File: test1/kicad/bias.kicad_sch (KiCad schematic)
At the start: 15 parts, among them Q40 PMZ1200UPEYL, Q41 PMZ1200UPEYL, Q42 2N7002, Q43 2N7002, U40 MCP4728, U41 OPA2388

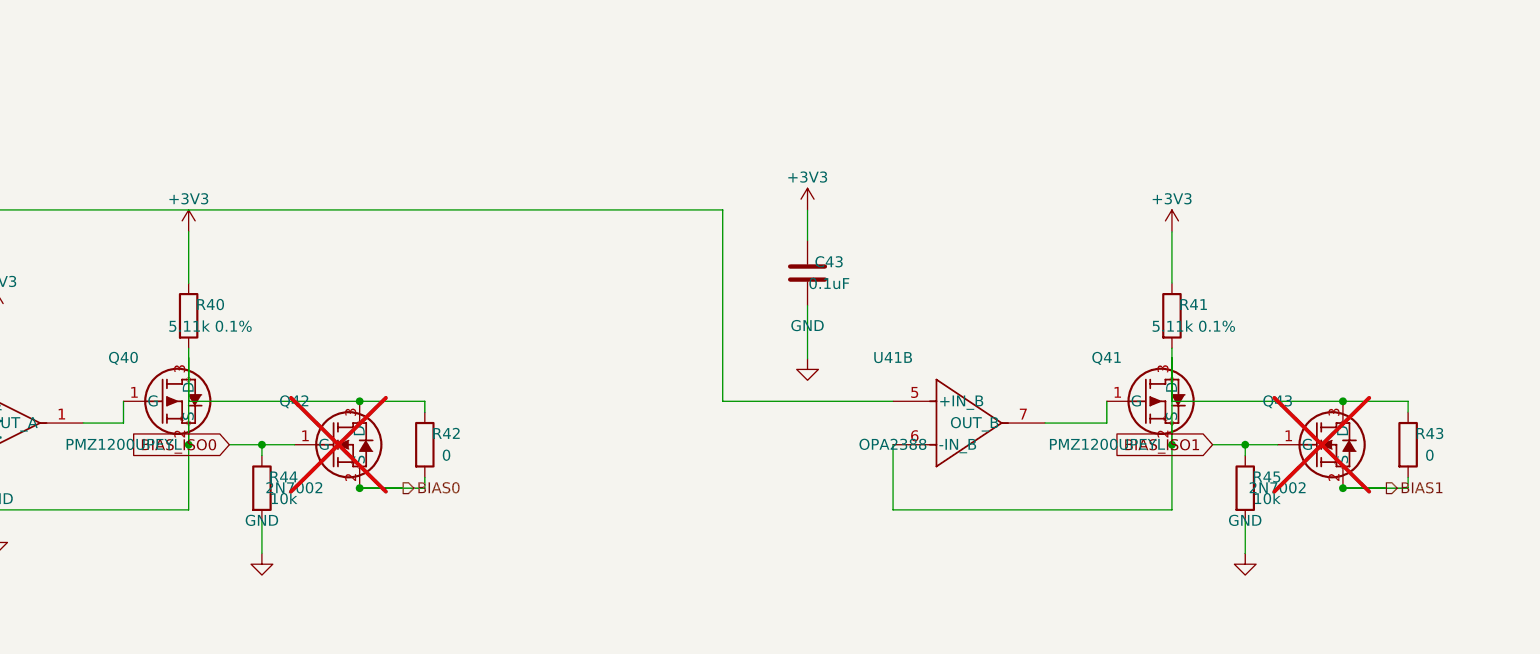
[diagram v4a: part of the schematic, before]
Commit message: Add layout linter + cluster helpers; fix silent shorts across sheets
Introduces gen/layout_lint.py with checks for bbox spacing, wires
through/into a body, parallel-wire overlap on the same axis, bridged
drop columns, and dense GND clusters — non-fatal warnings the strict
validator cannot catch (each net's name is still present in a bridged
component's name set, so per-member name checks pass).

Fixes the bugs the linter exposed:
- FMC routing flipped to exit LEFT (pin-protrusion side) so wires no
  longer pass through the connector body
- bobcat OWT (pins 23-25) + GPIO (37-40) get one drop column per pin,
  ending the silent shorts between adjacent nets
- bobcat SPI pin 14 pull-x shifted off pin 19's column
- bias Q40/Q41 source/drain wires detoured around the body so source
  no longer shorts to drain through the same vertical
- power LDO redundant tap stubs + GND-rail dupes removed; C12 moved
  off R10's column so NR_SS doesn't short to GND
- C11 ↔ R10, J54-56 ↔ R50-52 spacing widened to meet bbox rule

Adds gnd_bus() and decoupling_cluster() helpers in gen/shared.py and
applies gnd_bus() to the eeprom address-strap pins.

Skill doc gets rules for pin-protrusion side, per-pin drop columns,
and same-axis wire overlap. All 7 sheets now pass kicad-cli parse,
the strict connectivity validator, and the layout linter.

Co-Authored-By: Claude Opus 4.7 (1M context) <noreply@anthropic.com>
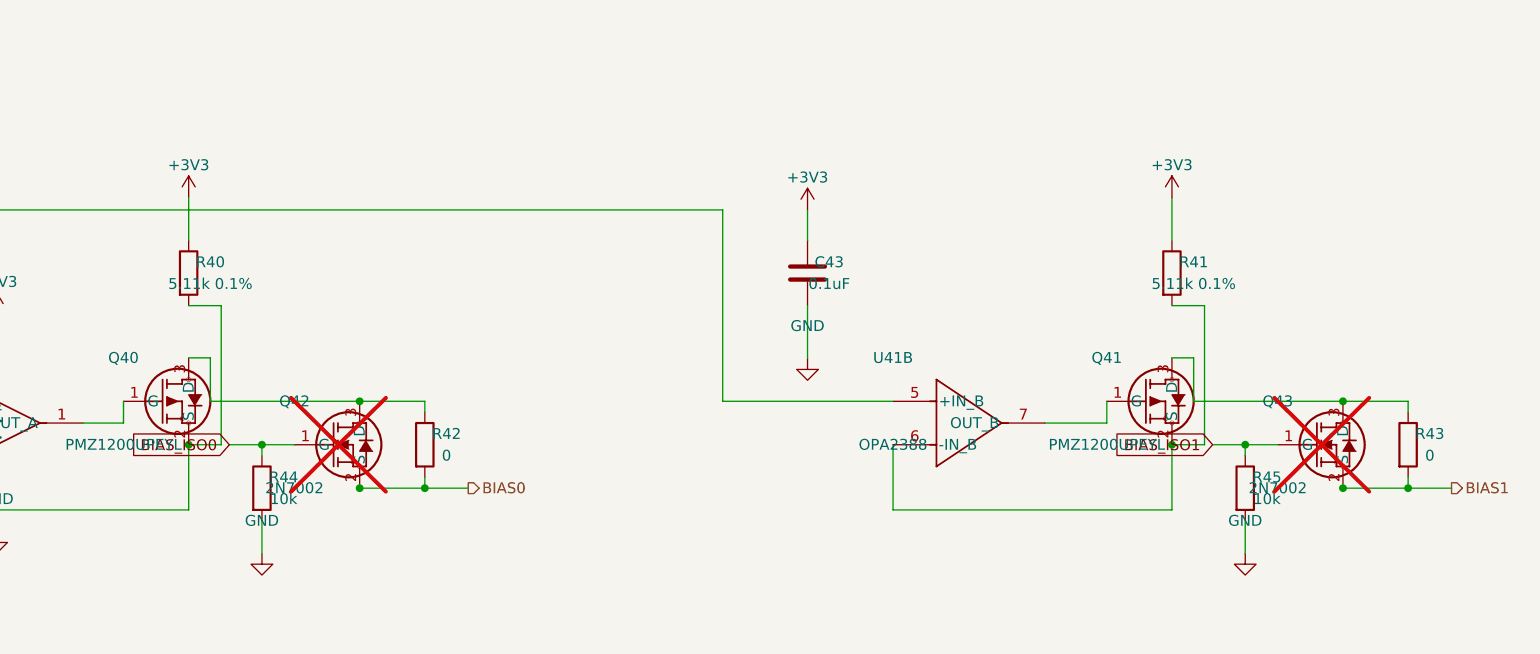
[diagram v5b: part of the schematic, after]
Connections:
- net at Q40.3 (D), Q42.3 (D), R42.1: no longer Q40.2 (S), R40.2, U41.2 (-IN_A)
- net at Q41.2 (S), R41.2, U41.6 (-IN_B): no longer Q41.3 (D), Q43.3 (D), R43.1
- new net: Q41.3 (D), Q43.3 (D), R43.1
- new net: Q40.2 (S), R40.2, U41.2 (-IN_A)
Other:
- moved on the sheet: R40, R41
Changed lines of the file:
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@@
   (symbol
     (lib_id "Device:R")
-    (at 237.62 100 0)
-    (unit 1) (in_bom yes) (on_board yes) (dnp no)
-    (property "Reference" "R40" (at 240.16 98.73 0) (effects (font (size 1.27 1.27))))
-    (property "Value" "5.11k 0.1%" (at 240.16 101.27 0) (effects (font (size 1.27 1.27))))
+    (at 237.62 95 0)
+    (unit 1) (in_bom yes) (on_board yes) (dnp no)
+    (property "Reference" "R40" (at 240.16 93.73 0) (effects (font (size 1.27 1.27))))
+    (property "Value" "5.11k 0.1%" (at 240.16 96.27 0) (effects (font (size 1.27 1.27))))
     (property "Footprint" "Resistor_SMD:R_0402_1005Metric" (at 0 0 0) (effects (font (size 1.27 1.27)) (hide yes)))
     (property "Datasheet" "" (at 0 0 0) (effects (font (size 1.27 1.27)) (hide yes)))
@@
       (project "test1"
         (path "/4ed7a046-ef33-57d9-8730-321c05965af3/ddf1c49f-55ac-530a-9ee4-38ad9d14caf8" (reference "R40") (unit 1)))))
-  (wire (pts (xy 237.62 103.81) (xy 237.62 115.08)) (stroke (width 0) (type default)))
-  (wire (pts (xy 237.62 96.19) (xy 237.62 90.17)) (stroke (width 0) (type default)))
-  (symbol
-    (lib_id "power:+3V3")
-    (at 237.62 90.17 0)
-    (unit 1) (in_bom yes) (on_board yes) (dnp no)
-    (property "Reference" "#PWR9abd0652" (at 237.62 83.82000000000001 0) (effects (font (size 1.27 1.27)) (hide yes)))
-    (property "Value" "+3V3" (at 237.62 86.36 0) (effects (font (size 1.27 1.27))))
-    (property "Footprint" "" (at 0 0 0) (effects (font (size 1.27 1.27)) (hide yes)))
-    (property "Datasheet" "" (at 0 0 0) (effects (font (size 1.27 1.27)) (hide yes)))
-    (pin "1")
-    (instances
-      (project "test1"
-        (path "/4ed7a046-ef33-57d9-8730-321c05965af3/ddf1c49f-55ac-530a-9ee4-38ad9d14caf8" (reference "#PWR9abd0652") (unit 1)))))
+  (wire (pts (xy 237.62 115.08) (xy 241.43 115.08)) (stroke (width 0) (type default)))
+  (wire (pts (xy 241.43 115.08) (xy 241.43 98.81)) (stroke (width 0) (type default)))
+  (wire (pts (xy 241.43 98.81) (xy 237.62 98.81)) (stroke (width 0) (type default)))
+  (wire (pts (xy 237.62 91.19) (xy 237.62 86.19)) (stroke (width 0) (type default)))
+  (symbol
+    (lib_id "power:+3V3")
+    (at 237.62 86.19 0)
+    (unit 1) (in_bom yes) (on_board yes) (dnp no)
+    (property "Reference" "#PWRa475a855" (at 237.62 79.84 0) (effects (font (size 1.27 1.27)) (hide yes)))
+    (property "Value" "+3V3" (at 237.62 82.38 0) (effects (font (size 1.27 1.27))))
+    (property "Footprint" "" (at 0 0 0) (effects (font (size 1.27 1.27)) (hide yes)))
+    (property "Datasheet" "" (at 0 0 0) (effects (font (size 1.27 1.27)) (hide yes)))
+    (pin "1")
+    (instances
+      (project "test1"
+        (path "/4ed7a046-ef33-57d9-8730-321c05965af3/ddf1c49f-55ac-530a-9ee4-38ad9d14caf8" (reference "#PWRa475a855") (unit 1)))))
   (wire (pts (xy 205.0 115.08) (xy 205.0 122.7)) (stroke (width 0) (type default)))
   (wire (pts (xy 205.0 122.7) (xy 237.62 122.7)) (stroke (width 0) (type default)))
@@
       (project "test1"
         (path "/4ed7a046-ef33-57d9-8730-321c05965af3/ddf1c49f-55ac-530a-9ee4-38ad9d14caf8" (reference "Q42") (unit 1)))))
-  (wire (pts (xy 237.62 104.92) (xy 237.62 110.0)) (stroke (width 0) (type default)))
-  (wire (pts (xy 237.62 110.0) (xy 257.62 110.0)) (stroke (width 0) (type default)))
-  (wire (pts (xy 257.62 120.16) (xy 262.7 120.16)) (stroke (width 0) (type default)))
-  (hierarchical_label "BIAS0" (shape output) (at 262.7 120.16 0) (effects (font (size 1.27 1.27)) (justify left)))
-  (wire (pts (xy 250.0 115.08) (xy 242.38 115.08)) (stroke (width 0) (type default)))
-  (global_label "BIAS_ISO0" (shape input) (at 242.38 115.08 180) (effects (font (size 1.27 1.27)) (justify right)))
+  (wire (pts (xy 237.62 104.92) (xy 240.16 104.92)) (stroke (width 0) (type default)))
+  (wire (pts (xy 240.16 104.92) (xy 240.16 110.0)) (stroke (width 0) (type default)))
+  (wire (pts (xy 240.16 110.0) (xy 257.62 110.0)) (stroke (width 0) (type default)))
   (symbol
     (lib_id "Device:R")
@@
   (wire (pts (xy 257.62 120.16) (xy 265.24 120.16)) (stroke (width 0) (type default)))
   (wire (pts (xy 265.24 120.16) (xy 265.24 118.89)) (stroke (width 0) (type default)))
+  (junction (at 265.24 120.16) (diameter 0) (color 0 0 0 0))
+  (wire (pts (xy 265.24 120.16) (xy 270.32 120.16)) (stroke (width 0) (type default)))
+  (hierarchical_label "BIAS0" (shape output) (at 270.32 120.16 0) (effects (font (size 1.27 1.27)) (justify left)))
+  (wire (pts (xy 250.0 115.08) (xy 242.38 115.08)) (stroke (width 0) (type default)))
+  (global_label "BIAS_ISO0" (shape input) (at 242.38 115.08 180) (effects (font (size 1.27 1.27)) (justify right)))
   (junction (at 246.19 115.08) (diameter 0) (color 0 0 0 0))
   (symbol
@@
   (symbol
     (lib_id "Device:R")
-    (at 352.62 100 0)
-    (unit 1) (in_bom yes) (on_board yes) (dnp no)
-    (property "Reference" "R41" (at 355.16 98.73 0) (effects (font (size 1.27 1.27))))
-    (property "Value" "5.11k 0.1%" (at 355.16 101.27 0) (effects (font (size 1.27 1.27))))
+    (at 352.62 95 0)
+    (unit 1) (in_bom yes) (on_board yes) (dnp no)
+    (property "Reference" "R41" (at 355.16 93.73 0) (effects (font (size 1.27 1.27))))
+    (property "Value" "5.11k 0.1%" (at 355.16 96.27 0) (effects (font (size 1.27 1.27))))
     (property "Footprint" "Resistor_SMD:R_0402_1005Metric" (at 0 0 0) (effects (font (size 1.27 1.27)) (hide yes)))
     (property "Datasheet" "" (at 0 0 0) (effects (font (size 1.27 1.27)) (hide yes)))
@@
       (project "test1"
         (path "/4ed7a046-ef33-57d9-8730-321c05965af3/ddf1c49f-55ac-530a-9ee4-38ad9d14caf8" (reference "R41") (unit 1)))))
-  (wire (pts (xy 352.62 103.81) (xy 352.62 115.08)) (stroke (width 0) (type default)))
-  (wire (pts (xy 352.62 96.19) (xy 352.62 90.17)) (stroke (width 0) (type default)))
-  (symbol
-    (lib_id "power:+3V3")
-    (at 352.62 90.17 0)
-    (unit 1) (in_bom yes) (on_board yes) (dnp no)
-    (property "Reference" "#PWRb943747a" (at 352.62 83.82000000000001 0) (effects (font (size 1.27 1.27)) (hide yes)))
-    (property "Value" "+3V3" (at 352.62 86.36 0) (effects (font (size 1.27 1.27))))
-    (property "Footprint" "" (at 0 0 0) (effects (font (size 1.27 1.27)) (hide yes)))
-    (property "Datasheet" "" (at 0 0 0) (effects (font (size 1.27 1.27)) (hide yes)))
-    (pin "1")
-    (instances
-      (project "test1"
-        (path "/4ed7a046-ef33-57d9-8730-321c05965af3/ddf1c49f-55ac-530a-9ee4-38ad9d14caf8" (reference "#PWRb943747a") (unit 1)))))
+  (wire (pts (xy 352.62 115.08) (xy 356.43 115.08)) (stroke (width 0) (type default)))
+  (wire (pts (xy 356.43 115.08) (xy 356.43 98.81)) (stroke (width 0) (type default)))
+  (wire (pts (xy 356.43 98.81) (xy 352.62 98.81)) (stroke (width 0) (type default)))
+  (wire (pts (xy 352.62 91.19) (xy 352.62 86.19)) (stroke (width 0) (type default)))
+  (symbol
+    (lib_id "power:+3V3")
+    (at 352.62 86.19 0)
+    (unit 1) (in_bom yes) (on_board yes) (dnp no)
+    (property "Reference" "#PWR16698b01" (at 352.62 79.84 0) (effects (font (size 1.27 1.27)) (hide yes)))
+    (property "Value" "+3V3" (at 352.62 82.38 0) (effects (font (size 1.27 1.27))))
+    (property "Footprint" "" (at 0 0 0) (effects (font (size 1.27 1.27)) (hide yes)))
+    (property "Datasheet" "" (at 0 0 0) (effects (font (size 1.27 1.27)) (hide yes)))
+    (pin "1")
+    (instances
+      (project "test1"
+        (path "/4ed7a046-ef33-57d9-8730-321c05965af3/ddf1c49f-55ac-530a-9ee4-38ad9d14caf8" (reference "#PWR16698b01") (unit 1)))))
   (wire (pts (xy 320.0 115.08) (xy 320.0 122.7)) (stroke (width 0) (type default)))
   (wire (pts (xy 320.0 122.7) (xy 352.62 122.7)) (stroke (width 0) (type default)))
@@
       (project "test1"
         (path "/4ed7a046-ef33-57d9-8730-321c05965af3/ddf1c49f-55ac-530a-9ee4-38ad9d14caf8" (reference "Q43") (unit 1)))))
-  (wire (pts (xy 352.62 104.92) (xy 352.62 110.0)) (stroke (width 0) (type default)))
-  (wire (pts (xy 352.62 110.0) (xy 372.62 110.0)) (stroke (width 0) (type default)))
-  (wire (pts (xy 372.62 120.16) (xy 377.7 120.16)) (stroke (width 0) (type default)))
-  (hierarchical_label "BIAS1" (shape output) (at 377.7 120.16 0) (effects (font (size 1.27 1.27)) (justify left)))
-  (wire (pts (xy 365.0 115.08) (xy 357.38 115.08)) (stroke (width 0) (type default)))
-  (global_label "BIAS_ISO1" (shape input) (at 357.38 115.08 180) (effects (font (size 1.27 1.27)) (justify right)))
+  (wire (pts (xy 352.62 104.92) (xy 355.16 104.92)) (stroke (width 0) (type default)))
+  (wire (pts (xy 355.16 104.92) (xy 355.16 110.0)) (stroke (width 0) (type default)))
+  (wire (pts (xy 355.16 110.0) (xy 372.62 110.0)) (stroke (width 0) (type default)))
   (symbol
     (lib_id "Device:R")
@@
   (wire (pts (xy 372.62 120.16) (xy 380.24 120.16)) (stroke (width 0) (type default)))
   (wire (pts (xy 380.24 120.16) (xy 380.24 118.89)) (stroke (width 0) (type default)))
+  (junction (at 380.24 120.16) (diameter 0) (color 0 0 0 0))
+  (wire (pts (xy 380.24 120.16) (xy 385.32 120.16)) (stroke (width 0) (type default)))
+  (hierarchical_label "BIAS1" (shape output) (at 385.32 120.16 0) (effects (font (size 1.27 1.27)) (justify left)))
+  (wire (pts (xy 365.0 115.08) (xy 357.38 115.08)) (stroke (width 0) (type default)))
+  (global_label "BIAS_ISO1" (shape input) (at 357.38 115.08 180) (effects (font (size 1.27 1.27)) (justify right)))
   (junction (at 361.19 115.08) (diameter 0) (color 0 0 0 0))
   (symbol
